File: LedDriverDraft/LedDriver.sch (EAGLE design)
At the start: 30 parts, among them IC1 TPS63020DSJR, IC2 MCP602ST

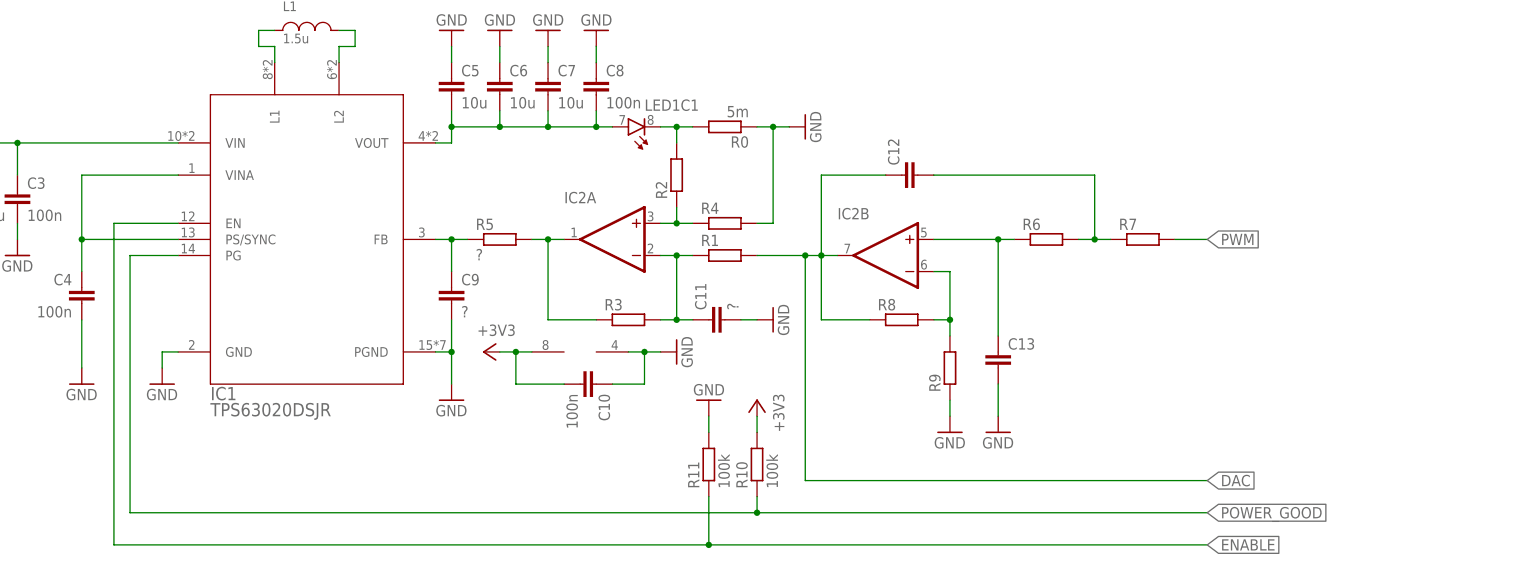
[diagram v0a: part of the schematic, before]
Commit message: Add values, but no suitable (fast enough) OP AMP found.
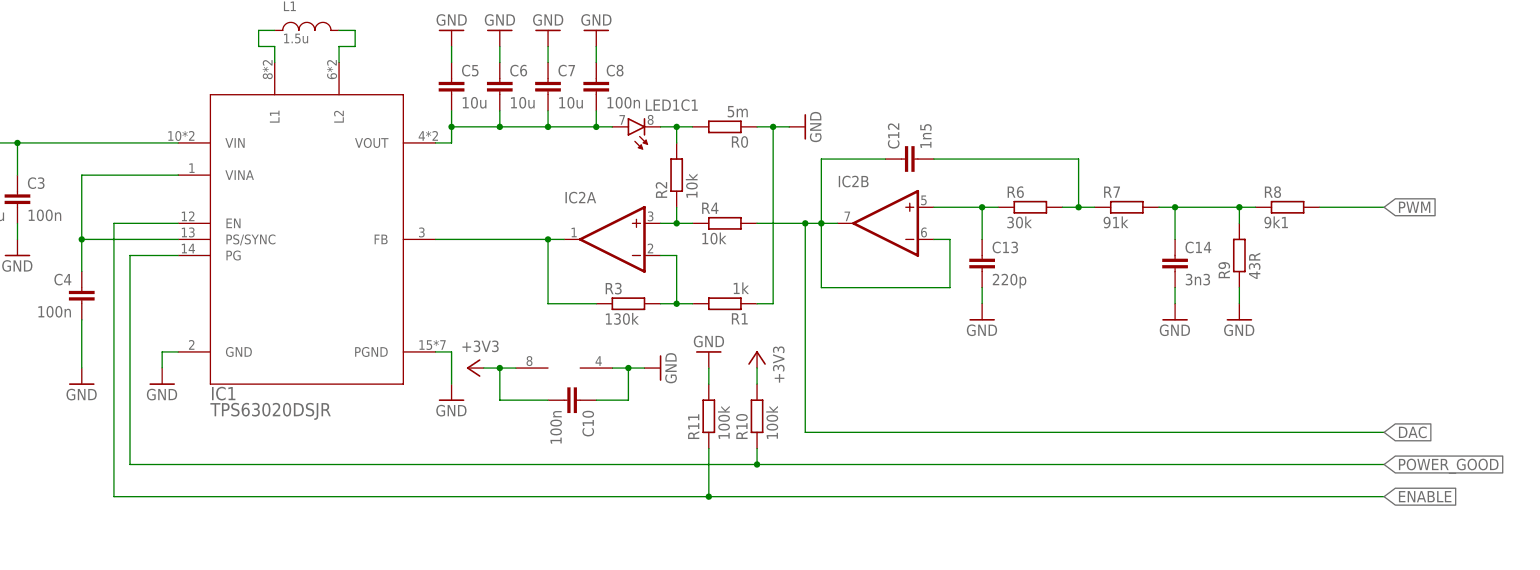
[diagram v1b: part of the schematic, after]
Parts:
- removed C11, C9: ?, rcl_upravena:C-EUC0402
- removed R5: ?, rcl_upravena:R-EU_R0402
- added C14: 3n3, rcl_upravena:C-EUC0402
- C12: value (none) -> 1n5
- C13: value (none) -> 220p
- R1: value (none) -> 1k
- R2, R4: value (none) -> 10k
- R3: value (none) -> 130k
- R6: value (none) -> 30k
- R7: value (none) -> 91k
- R8: value (none) -> 9k1
- R9: value (none) -> 43R
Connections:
- removed net FB_FILT: C9.1, IC1.FB, R5.1
- removed net N$4: IC2B.-IN, R8.2, R9.2
- new net N$2: C14.1, R7.2, R8.1, R9.2
- net DAC: now also IC2B.-IN, R4.2; no longer R1.2, R8.1
- net FB: now also IC1.FB; no longer R5.2
- net GND: now also C14.2, R1.1; no longer C11.2, C9.2, R4.2
- net PWM: now also R8.2; no longer R7.2
- net VA: now also R1.2; no longer C11.1, R1.1
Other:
- moved on the sheet: C10, C12, C13, IC2B, R1, R10, R11, R3, R6, R7, R8, R9

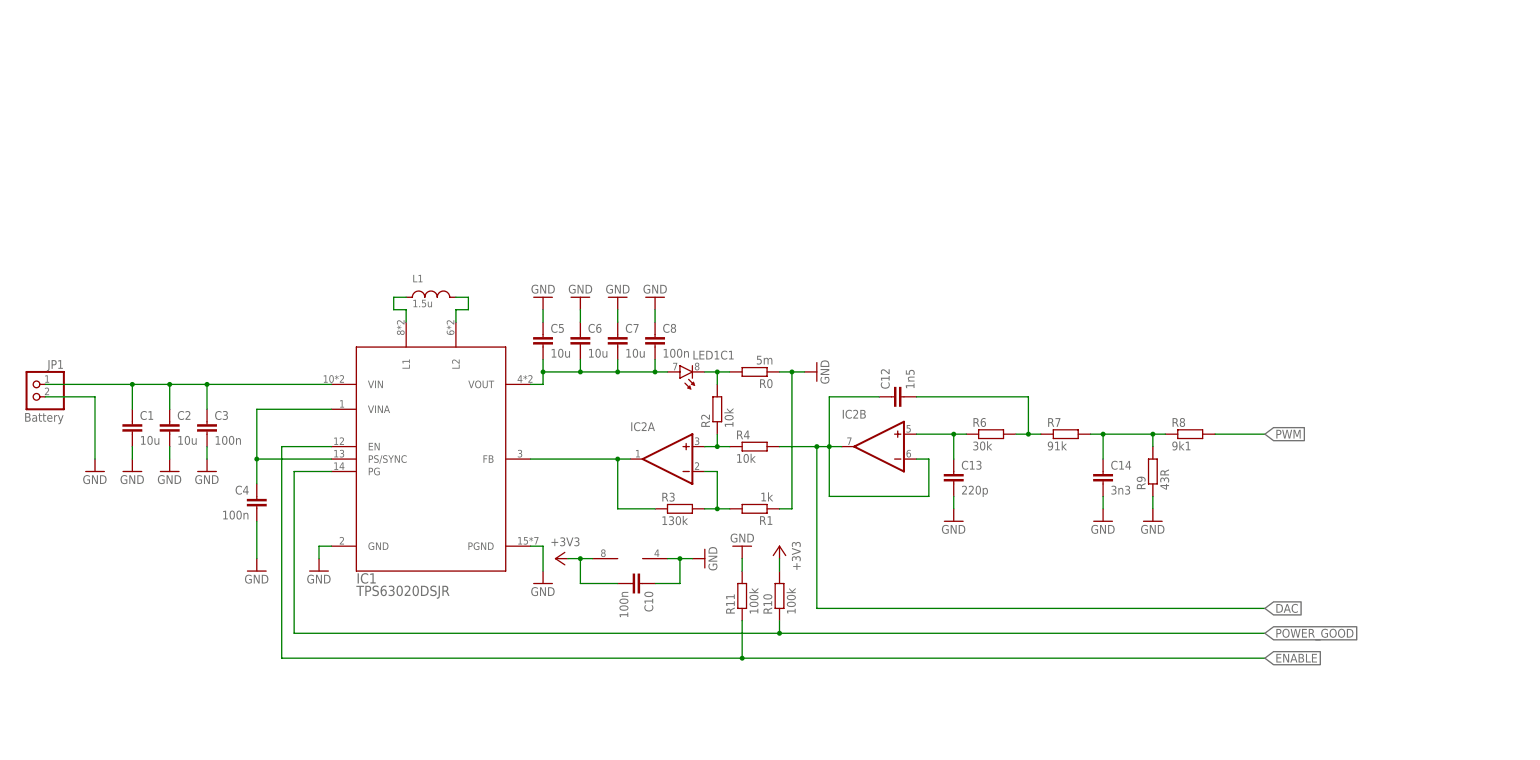
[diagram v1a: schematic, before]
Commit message: Redesign for slower OP AMPs, choose parts
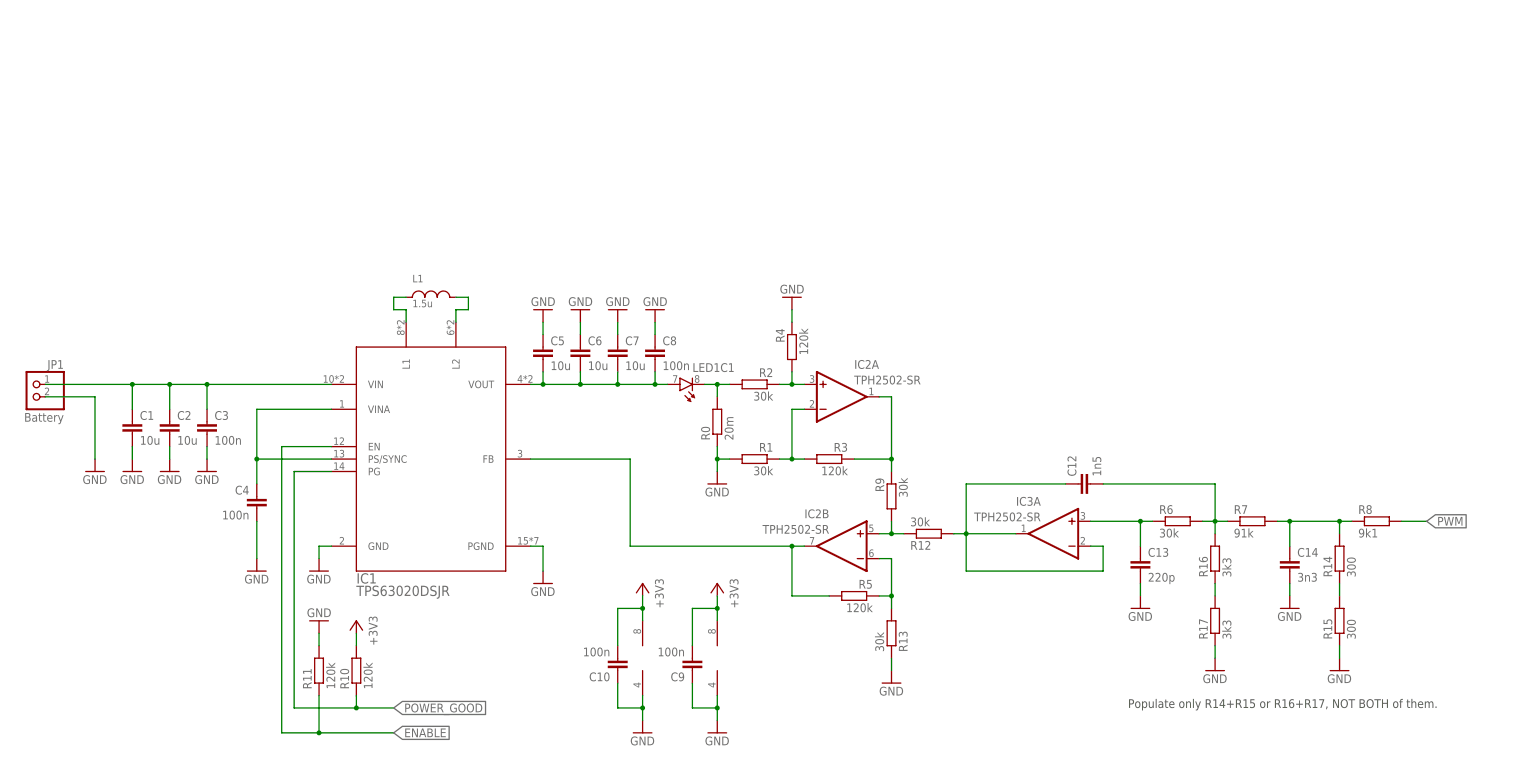
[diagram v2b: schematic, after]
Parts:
- added C9: 100n, rcl_upravena:C-EUC0603
- added IC3: TPH2502-SR, linear_upravena:MCP602ST
- added R12, R13: 30k, rcl_upravena:R-EU_R0603
- added R14, R15: 300, rcl_upravena:R-EU_R0603
- added R16, R17: 3k3, rcl_upravena:R-EU_R0603
- added R5: 120k, rcl_upravena:R-EU_R0603
- C1, C2, C5, C6, C7: LCSC (none) -> C96446
- C10, C3, C4, C8: device rcl_upravena:C-EUC0402 -> rcl_upravena:C-EUC0603; LCSC (none) -> C14663
- C12: device rcl_upravena:C-EUC0402 -> rcl_upravena:C-EUC0603; LCSC (none) -> C1595
- C13: device rcl_upravena:C-EUC0402 -> rcl_upravena:C-EUC0603; LCSC (none) -> C1603
- C14: device rcl_upravena:C-EUC0402 -> rcl_upravena:C-EUC0603; LCSC (none) -> C1613
- IC1: LCSC (none) -> C15483
- IC2: value MCP602ST -> TPH2502-SR; LCSC (none) -> C118223
- L1: LCSC (none) -> C408344
- R0: value 5m -> 20m; LCSC (none) -> C92740
- R1: value 1k -> 30k; device rcl_upravena:R-EU_R0402 -> rcl_upravena:R-EU_R0603; LCSC (none) -> C22984
- R10, R11: value 100k -> 120k; LCSC (none) -> C25808
- R2: value 10k -> 30k; device rcl_upravena:R-EU_R0402 -> rcl_upravena:R-EU_R0603; LCSC (none) -> C22984
- R3: value 130k -> 120k; device rcl_upravena:R-EU_R0402 -> rcl_upravena:R-EU_R0603; LCSC (none) -> C25808
- R4: value 10k -> 120k; device rcl_upravena:R-EU_R0402 -> rcl_upravena:R-EU_R0603; LCSC (none) -> C25808
- R6: device rcl_upravena:R-EU_R0402 -> rcl_upravena:R-EU_R0603; LCSC (none) -> C22984
- R7: device rcl_upravena:R-EU_R0402 -> rcl_upravena:R-EU_R0603; LCSC (none) -> C23265
- R8: device rcl_upravena:R-EU_R0402 -> rcl_upravena:R-EU_R0603; LCSC (none) -> C23260
- R9: value 43R -> 30k; device rcl_upravena:R-EU_R0402 -> rcl_upravena:R-EU_R0603; LCSC (none) -> C22984
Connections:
- removed net DAC: C12.1, IC2B.-IN, IC2B.OUT, R4.2
- new net N$10: R16.1, R17.2
- new net N$4: IC2B.-IN, R13.2, R5.1
- new net N$6: IC2A.OUT, R3.1, R9.1
- new net N$7: C13.1, IC3A.+IN, R6.1
- new net N$8: C12.1, IC3A.-IN, IC3A.OUT, R12.2
- new net N$9: R14.1, R15.2
- net +3V3: now also C9.2, IC3P.V+
- net FB: now also IC2B.OUT, R5.2; no longer IC2A.OUT, R3.1
- net GND: now also C9.1, IC3P.V-, R1.2, R13.1, R15.1, R17.1, R4.1; no longer R1.1, R9.1
- net N$1: now also R4.2; no longer R4.1
- net N$2: now also R14.2; no longer R9.2
- net N$3: now also R12.1, R9.2; no longer C13.1, R6.1
- net N$5: now also R16.2
- net VA: now also R1.1; no longer R1.2
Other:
- note added: "Populate only R14+R15 or R16+R17, NOT BOTH of them."
- moved on the sheet: C10, C12, C13, C14, C5, C6, C7, C8, IC2A, IC2B, LED1C1, R0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

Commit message: Fix filter attenuation, add fast dimming input
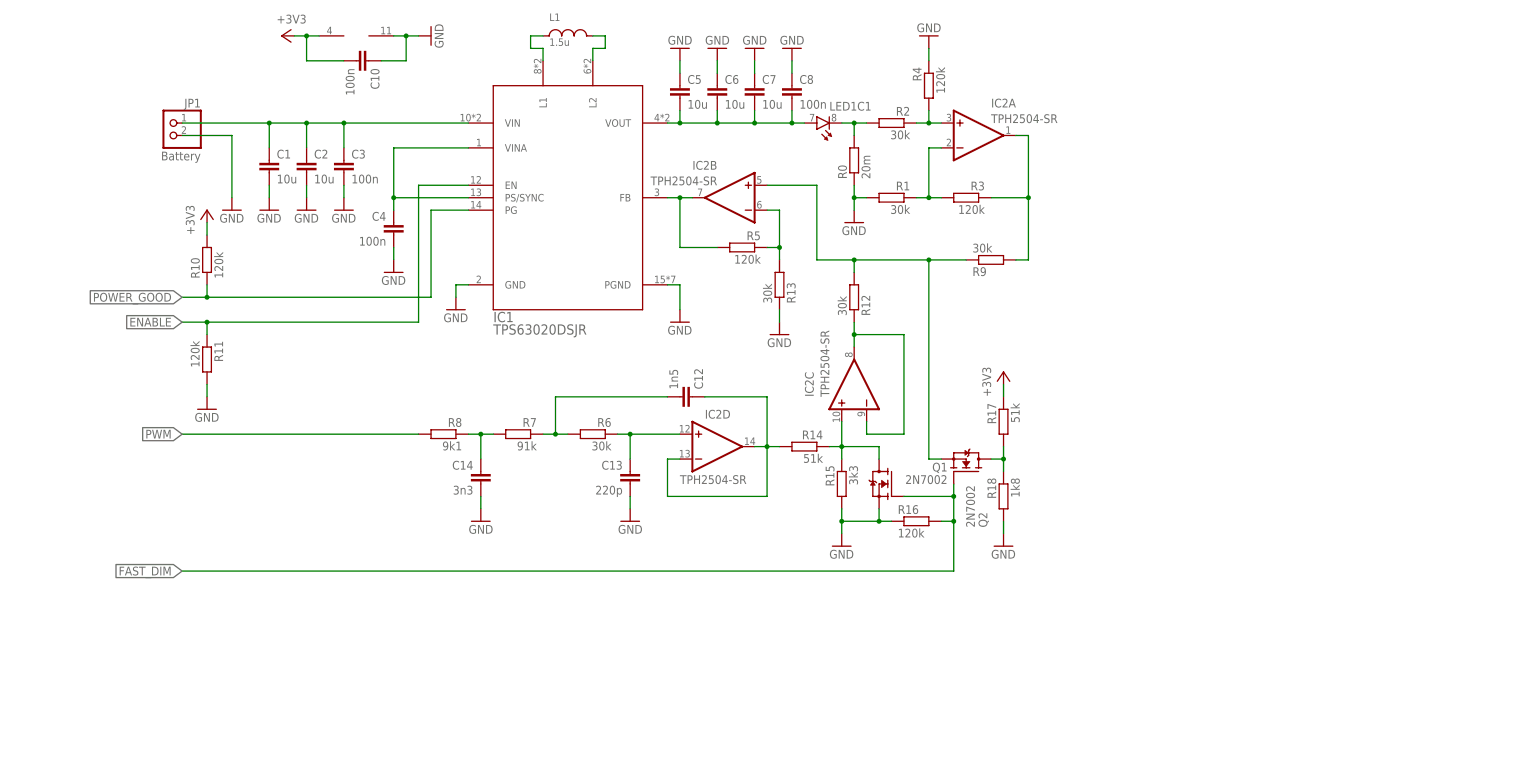
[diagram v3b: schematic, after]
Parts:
- removed C9: 100n, rcl_upravena:C-EUC0603
- removed IC3: TPH2502-SR, linear_upravena:MCP602ST
- added Q1, Q2: 2N7002, transistors:N-MOSFET-SOT23-GSD
- added R18: 1k8, rcl_upravena:R-EU_R0603
- IC2: value TPH2502-SR -> TPH2504-SR; device linear_upravena:MCP602ST -> linear_upravena:MCP604SL; LCSC C118223 -> C115918
- R14: value 300 -> 51k; LCSC C23025 -> C23196
- R15: value 300 -> 3k3; LCSC C23025 -> C22978
- R16: value 3k3 -> 120k; device rcl_upravena:R-EU_R0603 -> rcl_upravena:R-EU_R0402; LCSC C22978 -> C25808
- R17: value 3k3 -> 51k; LCSC C22978 -> C23196
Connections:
- new net FAST_DIM: Q1.G, Q2.G, R16.2
- new net N$12: Q2.D, R17.2, R18.1
- net +3V3: now also R17.1; no longer C9.2, IC3P.V+
- net GND: now also Q1.S, R15.2, R16.1, R18.2; no longer C9.1, IC3P.V-, R15.1, R17.1
- net N$10: now also IC2C.-IN, IC2C.OUT, R12.1; no longer R16.1, R17.2
- net N$2: no longer R14.2
- net N$3: now also Q2.S, R12.2, R9.1; no longer R12.1, R9.2
- net N$5: no longer R16.2
- net N$6: now also R9.2; no longer R9.1
- net N$7: now also IC2D.+IN; no longer IC3A.+IN
- net N$8: now also IC2D.-IN, IC2D.OUT, R14.2; no longer IC3A.-IN, IC3A.OUT, R12.2
- net N$9: now also IC2C.+IN, Q1.D, R15.1; no longer R15.2
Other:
- note removed: "Populate only R14+R15 or R16+R17, NOT BOTH of them."
- moved on the sheet: C1, C10, C12, C13, C14, C2, C3, C4, C5, C6, C7, C8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
